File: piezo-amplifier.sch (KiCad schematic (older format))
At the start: 62 parts, among them J1 AudioJack4, J2 AudioJack4, J3 AudioJack4, J4 AudioJack4, J5 Conn_01x03_Male, J6 Conn_02x05_Odd_Even, SW1 734-7081, SW2 734-7081, U1 NE5532, U2 NE5532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

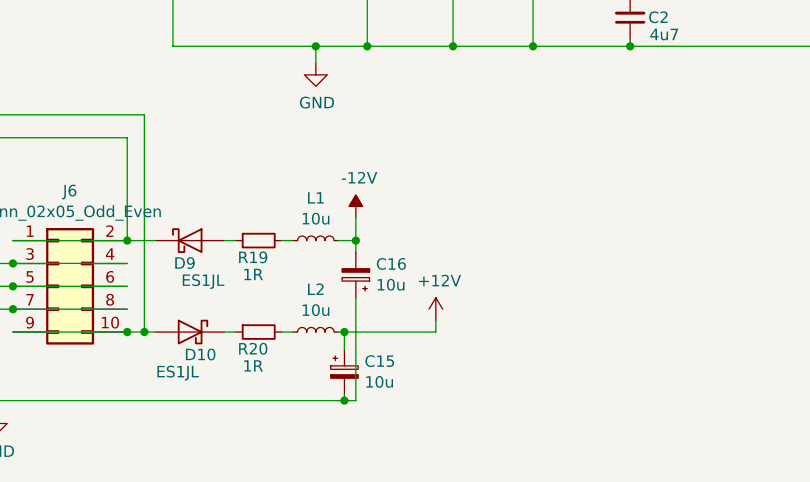
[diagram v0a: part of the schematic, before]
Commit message: switched to SMD capacitors, minor layout and silkscreen changes
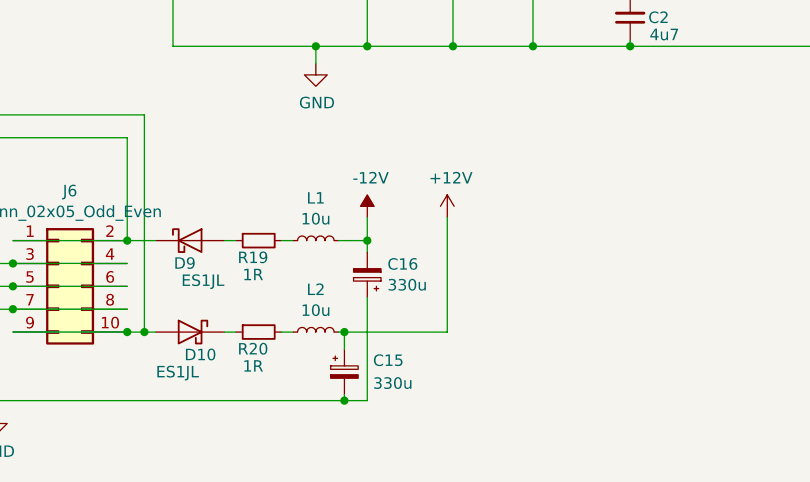
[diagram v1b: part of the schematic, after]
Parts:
- C15, C16: value 10u -> 330u; footprint Capacitor_THT:CP_Radial_D4.0mm_P2.00mm -> Capacitor_SMD:CP_Elec_8x10
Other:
- moved on the sheet: C16
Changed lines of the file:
@@
 Connection ~ 1650 6675
 Wire Wire Line
-	3225 6425 3225 6375
+	3275 6425 3275 6375
 Wire Wire Line
-	3225 6375 3150 6375
+	3275 6375 3150 6375
 Wire Wire Line
-	3225 6625 3225 7075
+	3275 6625 3275 7075
 Wire Wire Line
-	3225 7075 3175 7075
+	3275 7075 3175 7075
 Wire Wire Line
 	3175 7075 3175 7050
@@
 L power:+12V #PWR0122
 U 1 1 5D439A85
-P 3575 6725
-F 0 "#PWR0122" H 3575 6575 50  0001 C CNN
-F 1 "+12V" H 3590 6898 50  0000 C CNN
-F 2 "" H 3575 6725 50  0001 C CNN
-F 3 "" H 3575 6725 50  0001 C CNN
-	1    3575 6725
+P 3625 6275
+F 0 "#PWR0122" H 3625 6125 50  0001 C CNN
+F 1 "+12V" H 3640 6448 50  0000 C CNN
+F 2 "" H 3625 6275 50  0001 C CNN
+F 3 "" H 3625 6275 50  0001 C CNN
+	1    3625 6275
 	1    0    0    -1
 $EndComp
 Wire Wire Line
-	3575 6725 3575 6775
+	3625 6275 3625 6775
 Wire Wire Line
-	3575 6775 3175 6775
+	3625 6775 3175 6775
 Connection ~ 3175 6775
 $Comp
 L power:-12V #PWR0123
 U 1 1 5D45593D
-P 3225 6275
-F 0 "#PWR0123" H 3225 6375 50  0001 C CNN
-F 1 "-12V" H 3240 6448 50  0000 C CNN
-F 2 "" H 3225 6275 50  0001 C CNN
-F 3 "" H 3225 6275 50  0001 C CNN
-	1    3225 6275
+P 3275 6275
+F 0 "#PWR0123" H 3275 6375 50  0001 C CNN
+F 1 "-12V" H 3290 6448 50  0000 C CNN
+F 2 "" H 3275 6275 50  0001 C CNN
+F 3 "" H 3275 6275 50  0001 C CNN
+	1    3275 6275
 	1    0    0    -1
 $EndComp
 Wire Wire Line
-	3225 6275 3225 6375
-Connection ~ 3225 6375
+	3275 6275 3275 6375
+Connection ~ 3275 6375
 $Comp
 L Connector:Conn_01x03_Male J5
@@
 L Device:CP_Small C16
 U 1 1 5D4A02D8
-P 3225 6525
-F 0 "C16" H 3137 6479 50  0000 R CNN
-F 1 "10u" H 3137 6570 50  0000 R CNN
-F 2 "Capacitor_THT:CP_Radial_D4.0mm_P2.00mm" H 3225 6525 50  0001 C CNN
-F 3 "~" H 3225 6525 50  0001 C CNN
-	1    3225 6525
+P 3275 6525
+F 0 "C16" H 3187 6479 50  0000 R CNN
+F 1 "330u" H 3187 6570 50  0000 R CNN
+F 2 "Capacitor_SMD:CP_Elec_8x10" H 3275 6525 50  0001 C CNN
+F 3 "~" H 3275 6525 50  0001 C CNN
+	1    3275 6525
 	-1   0    0    1
 $EndComp
@@
 U 1 1 5D4A14CF
 P 3175 6950
-F 0 "C15" H 3263 6996 50  0000 L CNN
-F 1 "10u" H 3263 6905 50  0000 L CNN
-F 2 "Capacitor_THT:CP_Radial_D4.0mm_P2.00mm" H 3175 6950 50  0001 C CNN
+F 0 "C15" H 3300 7000 50  0000 L CNN
+F 1 "330u" H 3300 6900 50  0000 L CNN
+F 2 "Capacitor_SMD:CP_Elec_8x10" H 3175 6950 50  0001 C CNN
 F 3 "~" H 3175 6950 50  0001 C CNN
 	1    3175 6950
